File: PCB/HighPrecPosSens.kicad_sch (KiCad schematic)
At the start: 85 parts, among them J1 Conn_01x02_Male, J2 Conn_01x02_Male, J3 Conn_01x02_Male, J4 Conn_01x02_Male, J5 Conn_01x06_Male, U1 ST1S14PHR, U2 S12443, U3 LM393DR2G, U4 LM393DR2G, U5 74LVC541A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

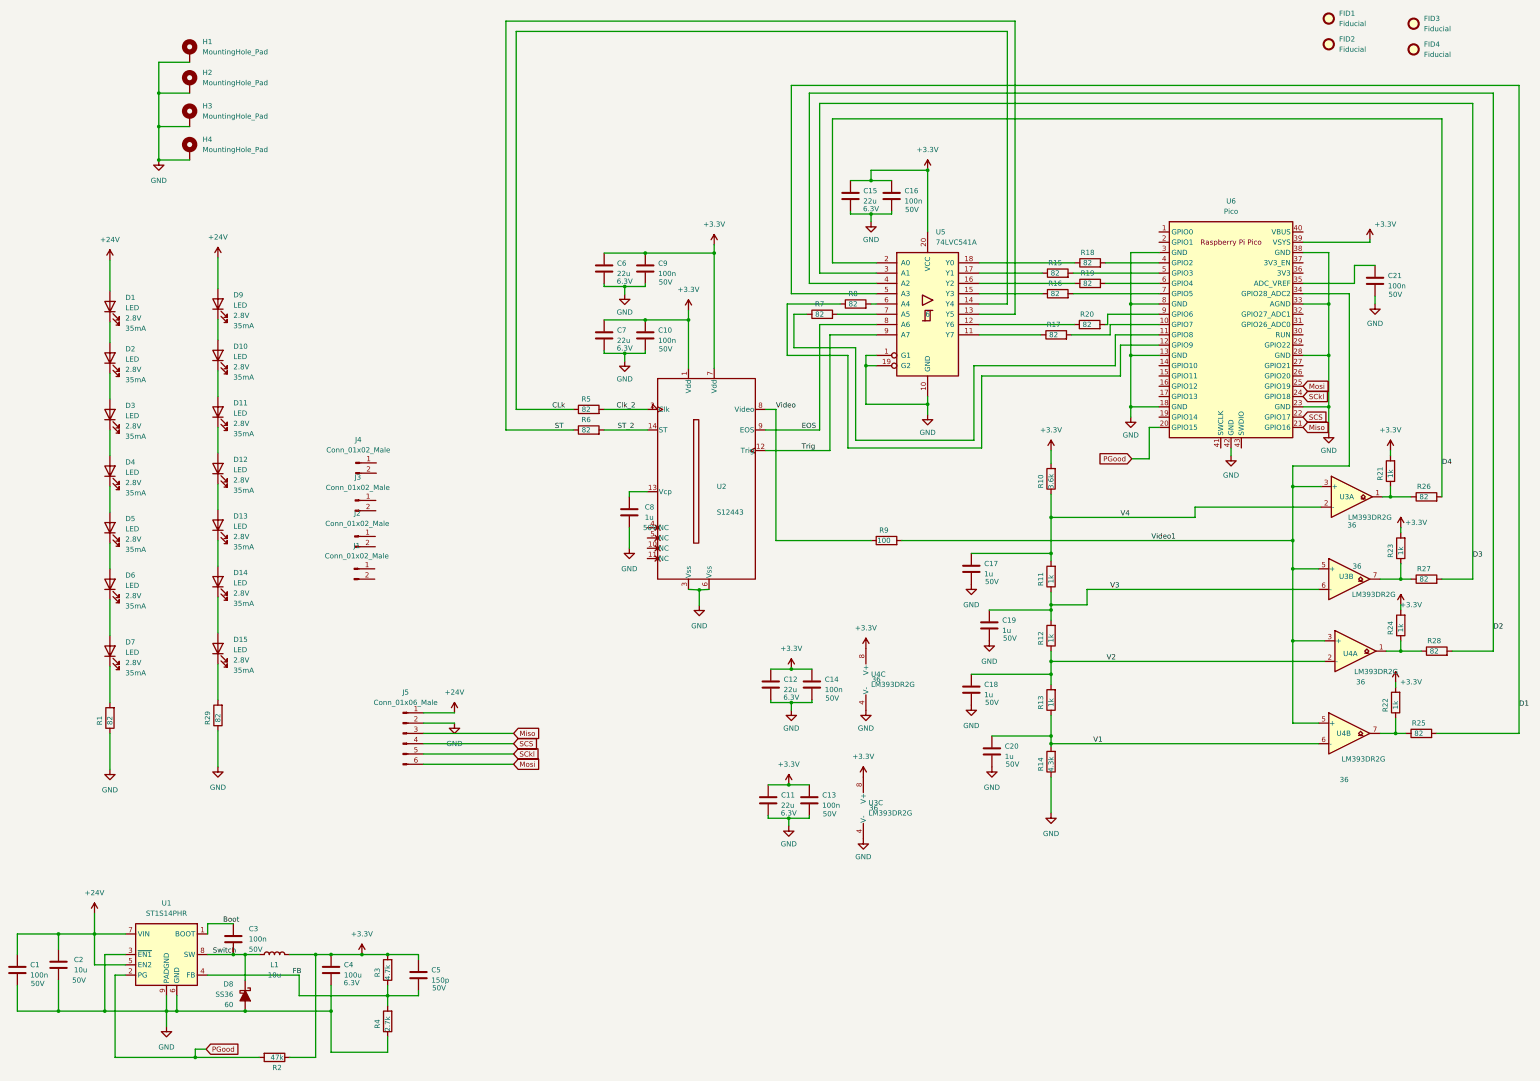
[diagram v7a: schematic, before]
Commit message: Added some reasonable testpoints
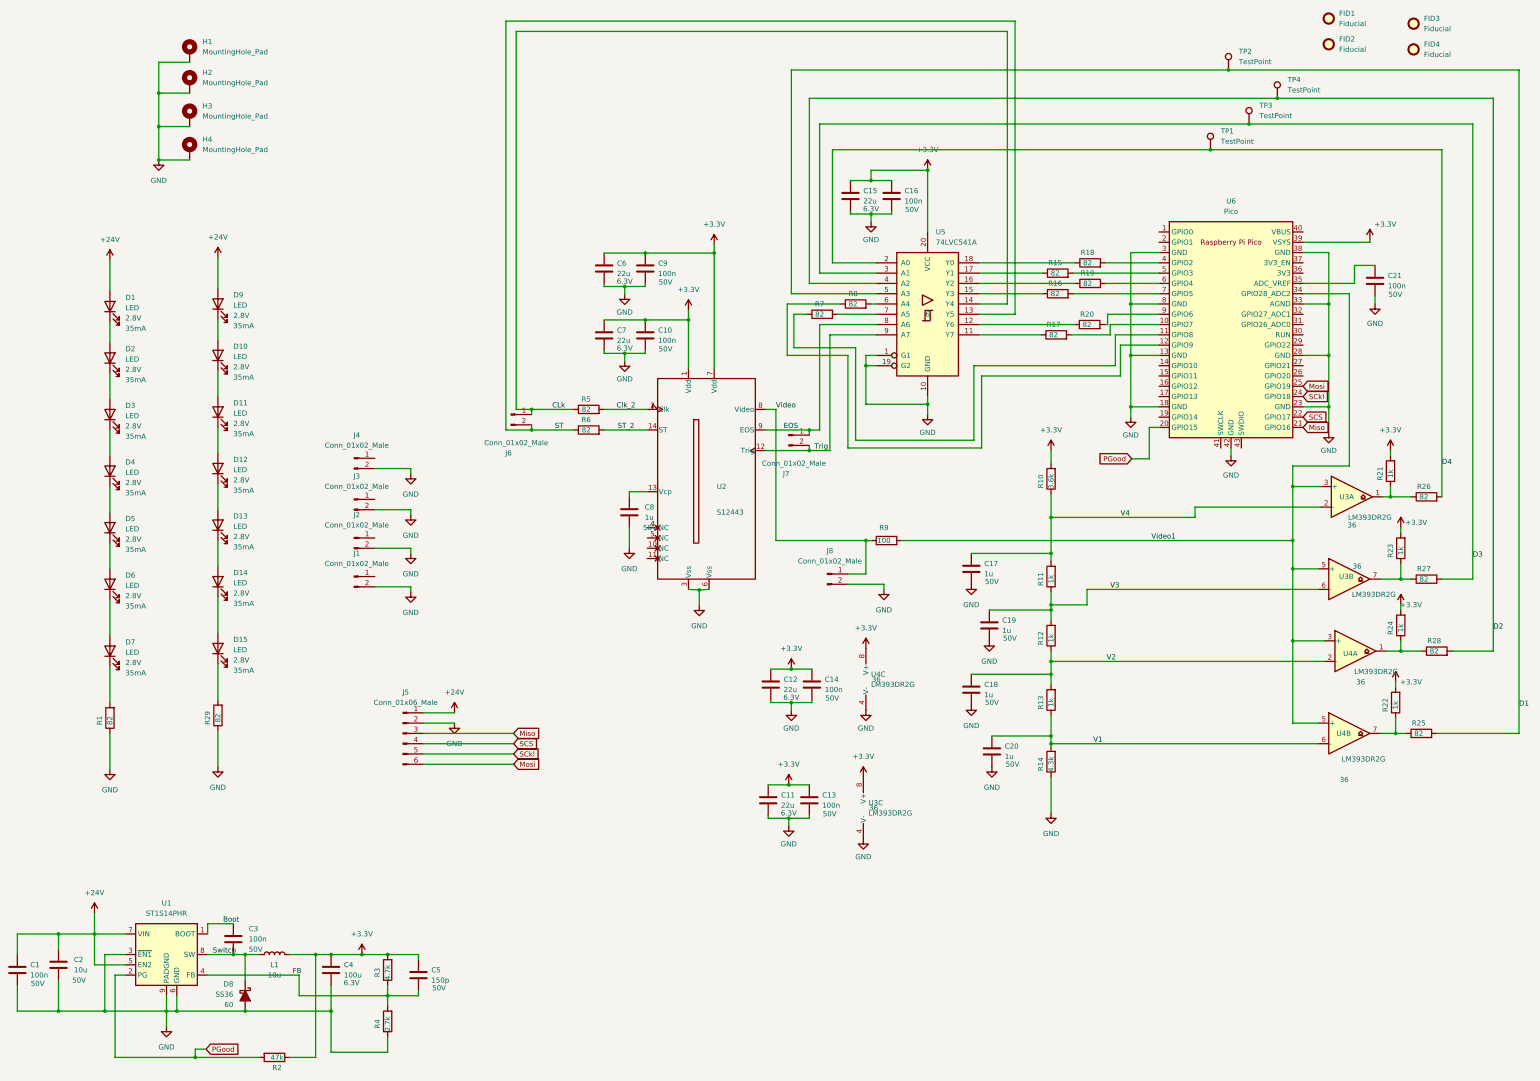
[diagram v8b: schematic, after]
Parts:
- added J6, J7, J8: Conn_01x02_Male, Connector_PinHeader_2.54mm:PinHeader_1x02_P2.54mm_Vertical, symbol Connector:Conn_01x02_Male
- added TP1, TP2, TP3, TP4: TestPoint, TestPoint:TestPoint_THTPad_D1.5mm_Drill0.7mm, symbol Connector:TestPoint
- J5: Mounting (none) -> DNP
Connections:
- net CLk: now also J6.1 (Pin_1)
- net D1: now also TP2.1
- net D2: now also TP4.1
- net D3: now also TP3.1
- net D4: now also TP1.1
- net EOS: now also J7.1 (Pin_1)
- net GND: now also J1.2 (Pin_2), J2.2 (Pin_2), J3.2 (Pin_2), J4.2 (Pin_2), J8.2 (Pin_2)
- net ST: now also J6.2 (Pin_2)
- net Trig: now also J7.2 (Pin_2)
- net Video: now also J8.1 (Pin_1)
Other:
- moved on the sheet: J1, J4
